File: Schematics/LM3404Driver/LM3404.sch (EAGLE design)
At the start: 62 parts, among them IC1 LM3404, IC2 LM3404, IC3 LM3404, IC4 LM3404, IC5 LM3404, IC6 LM3404

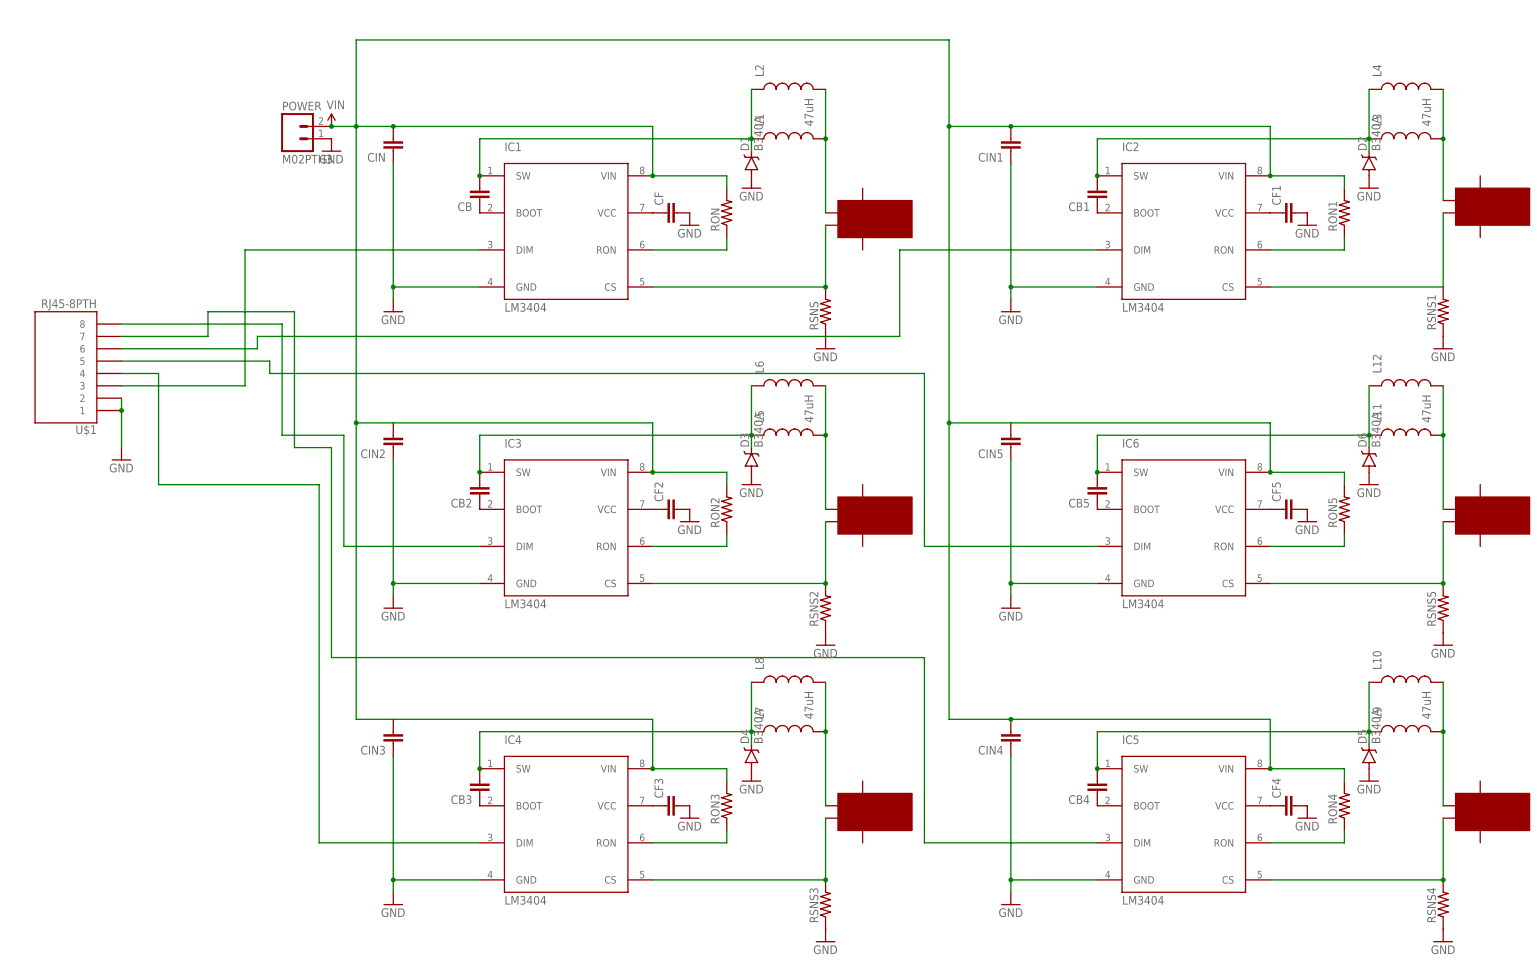
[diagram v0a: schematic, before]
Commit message: Update power driver board to smt RJ45 and correct ground pins
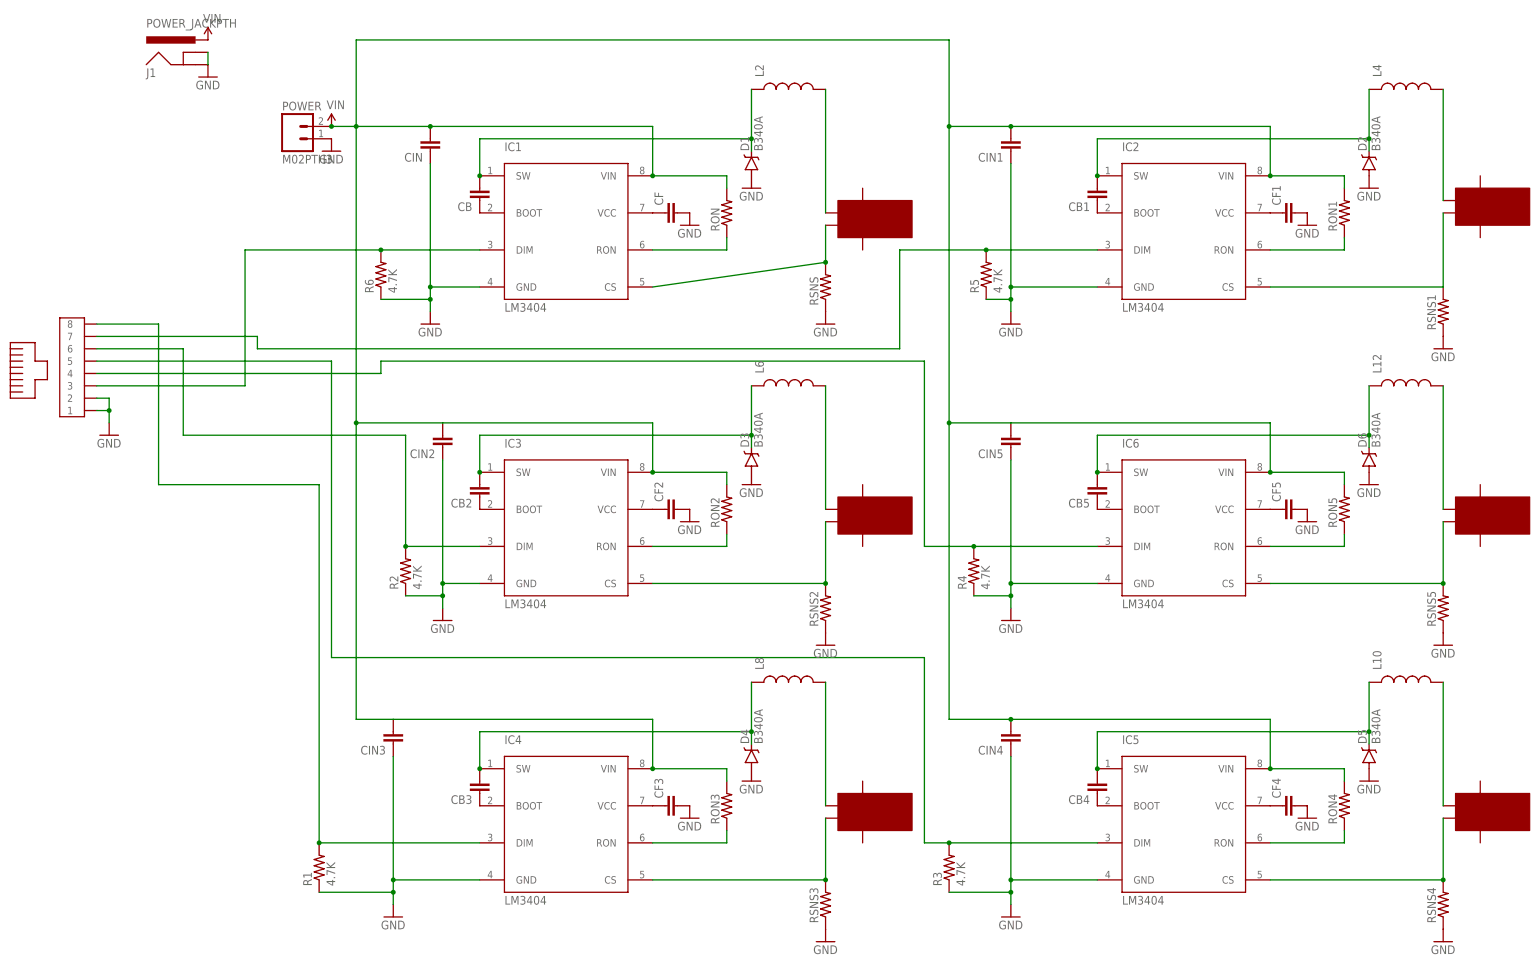
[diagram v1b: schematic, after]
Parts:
- removed L1, L11, L3, L5, L7, L9: 47uH, SparkFun-Passives:INDUCTOR68UH-1A
- added J1: POWER_JACKPTH, SparkFun-Connectors:POWER_JACKPTH
- added R1, R2, R3, R4, R5, R6: 4.7K, SparkFun-Resistors:RESISTOR1206
- U$1: value RJ45-8PTH -> MOLEX-RJ45-SMT; device SparkFun-Connectors:RJ45-8PTH -> SMD-RJ45:MOLEX-RJ45-SMT
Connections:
- net GND: now also J1.GND, J1.GNDBREAK, R1.1, R2.1, R3.1, R4.1, R5.1, R6.1
- net N$11: no longer L3.1
- net N$14: no longer L3.2
- net N$15: now also R2.2, U$1.6; no longer U$1.8
- net N$18: no longer L5.1
- net N$21: no longer L5.2
- net N$22: now also R1.2, U$1.8; no longer U$1.4
- net N$25: no longer L7.1
- net N$28: no longer L7.2
- net N$29: now also R3.2, U$1.5; no longer U$1.7
- net N$3: now also R5.2, U$1.7; no longer U$1.6
- net N$32: no longer L9.1
- net N$35: no longer L9.2
- net N$36: now also R4.2, U$1.4; no longer U$1.5
- net N$39: no longer L11.1
- net N$4: no longer L1.1
- net N$42: no longer L11.2
- net N$8: now also R6.2
- net N$9: no longer L1.2
- net VIN: now also J1.PWR
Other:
- moved on the sheet: CIN, CIN2, RSNS
